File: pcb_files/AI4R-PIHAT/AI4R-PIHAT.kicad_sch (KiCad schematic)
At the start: 15 parts, among them J1 Conn_02x20_Odd_Even, J2 Conn_01x04, J3 Conn_01x04, J4 Conn_01x04, J5 Conn_01x04, J6 Conn_02x10_Odd_Even, J7 Conn_01x03, J8 Conn_01x03, J9 Conn_01x02, U1 815

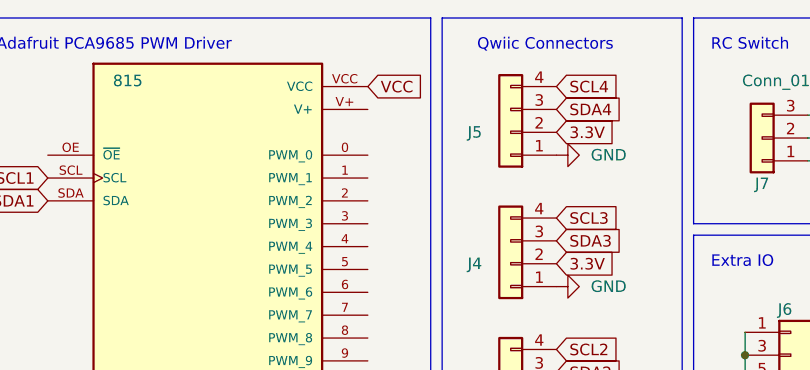
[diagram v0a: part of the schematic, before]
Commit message: fix gerber errors
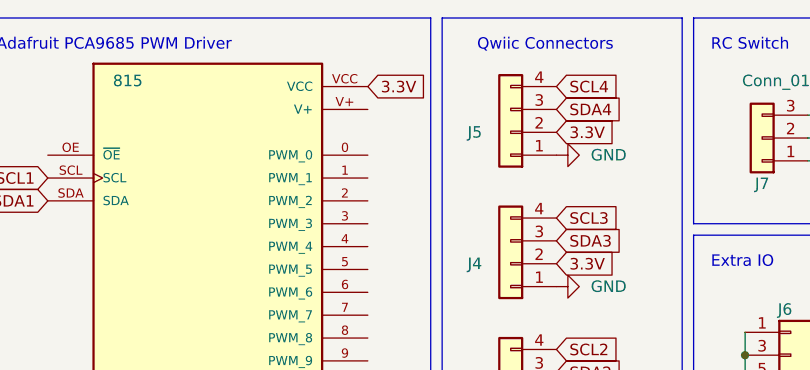
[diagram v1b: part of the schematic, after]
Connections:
- net 3.3V: now also U1.VCC
- net VCC: no longer U1.VCC
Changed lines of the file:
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@@
-    )
-  )
-  (global_label "VCC" (shape input) (at 112.395 24.13 0) (fields_autoplaced)
-    (effects (font (size 1.27 1.27)) (justify left))
-    (property "Intersheetrefs" "${INTERSHEET_REFS}" (at 119.0088 24.13 0)
-      (effects (font (size 1.27 1.27)) (justify left) hide)
     )
   )
@@
     )
   )
+  (global_label "3.3V" (shape input) (at 112.395 24.13 0) (fields_autoplaced)
+    (effects (font (size 1.27 1.27)) (justify left))
+    (property "Intersheetrefs" "${INTERSHEET_REFS}" (at 119.4926 24.13 0)
+      (effects (font (size 1.27 1.27)) (justify left) hide)
+    )
+  )
